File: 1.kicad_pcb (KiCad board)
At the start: 2 copper layers, 68.6 x 40.6 mm, 29 parts, among them J1 Screw_Terminal_01x03, J2 Screw_Terminal_01x01, J3 Screw_Terminal_01x01, J4 Conn_01x03_Pin, J5 Screw_Terminal_01x01, J6 Screw_Terminal_01x01, J7 Conn_01x01_Pin, J8 Conn_01x04_Pin, J9 Conn_01x01_Pin, U1 LTC2990

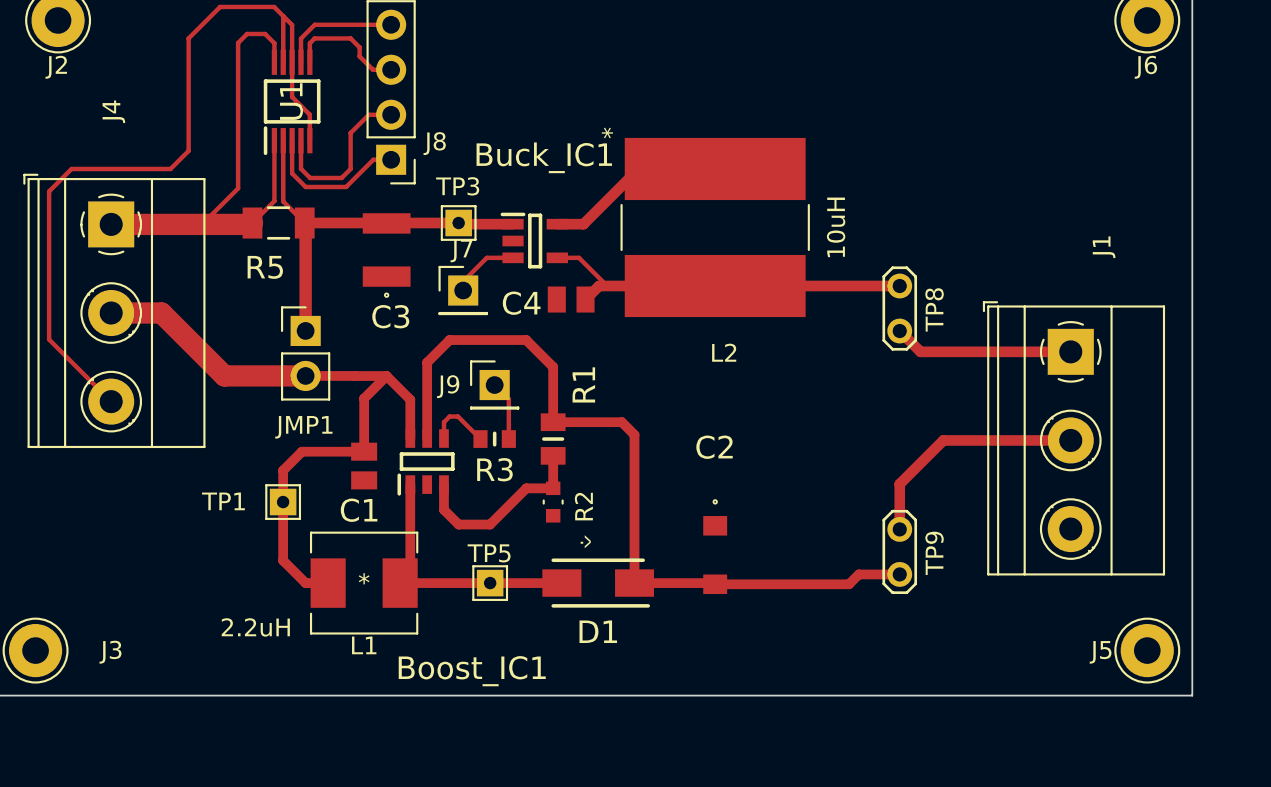
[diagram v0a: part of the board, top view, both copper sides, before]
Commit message: Add protection circ
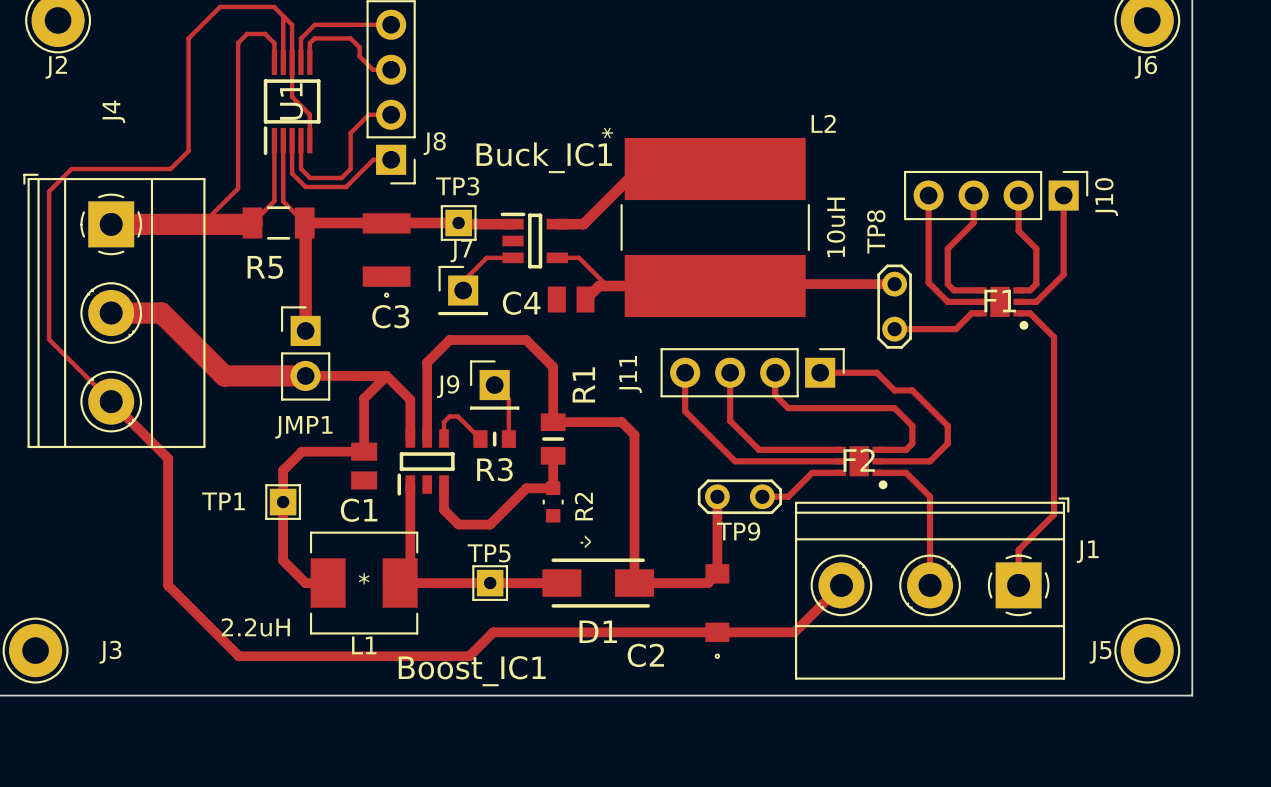
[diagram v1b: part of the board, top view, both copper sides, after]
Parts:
- added F1: TPS25961DRVR, PROTECC:SON65P200X200X80-7N, F.Cu at (166.9, 87.0)
- added F2: TPS25961DRVR, PROTECC:SON65P200X200X80-7N, F.Cu at (159.0, 96.0)
- added J10: Conn_01x04_Pin, Connector_PinHeader_2.54mm:PinHeader_1x04_P2.54mm_Vertical, F.Cu at (170.5, 81.0)
- added J11: Conn_01x04_Pin, Connector_PinHeader_2.54mm:PinHeader_1x04_P2.54mm_Vertical, F.Cu at (156.8, 91.0)
- moved J1 13.5 mm to (168.0, 103.0), turned to 180 degrees
- moved TP9 7.97 mm to (153.5, 98.0), turned to 180 degrees
- moved C2 2.71 mm to (151.0, 104.0), turned to 90 degrees
- moved TP8 0.31 mm to (161.0, 86.0)
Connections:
- J1 pad 1: Net-(J1-Pin_1) -> Net-(F1-OUT)
- J1 pad 2: Net-(J1-Pin_2) -> Net-(F2-OUT)
- TP8 pad 2: Net-(J1-Pin_1) -> Net-(F1-IN)
- TP9 pad 1: Net-(J1-Pin_2) -> Net-(F2-IN)
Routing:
- net Earth: track 45.0 -> 115.3 mm
- net Net-(F1-OUT): track 0.00 -> 17.4 mm
- net Net-(F2-OVLO): track 0.00 -> 13.8 mm
- net Net-(J1-Pin_2): track 13.2 -> 0.00 mm
- net Net-(F2-ILIM): track 0.00 -> 12.8 mm
- net Net-(F2-EN/UVLO): track 0.00 -> 12.1 mm
- net Net-(J1-Pin_1): track 10.1 -> 0.00 mm
- net Net-(F2-OUT): track 0.00 -> 8.51 mm
- net Net-(F1-EN/UVLO): track 0.00 -> 8.35 mm
- net Net-(F1-OVLO): track 0.00 -> 7.64 mm
- net Net-(F1-ILIM): track 0.00 -> 6.56 mm
- net Net-(Boost_IC1-VOUT): track 44.1 -> 38.2 mm
- net Net-(F1-IN): track 0.00 -> 5.27 mm
- net Net-(F2-IN): track 0.00 -> 4.97 mm
